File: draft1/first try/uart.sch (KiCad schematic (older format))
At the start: 24 parts, among them J1 47346-0001, U3 FT231XS-U

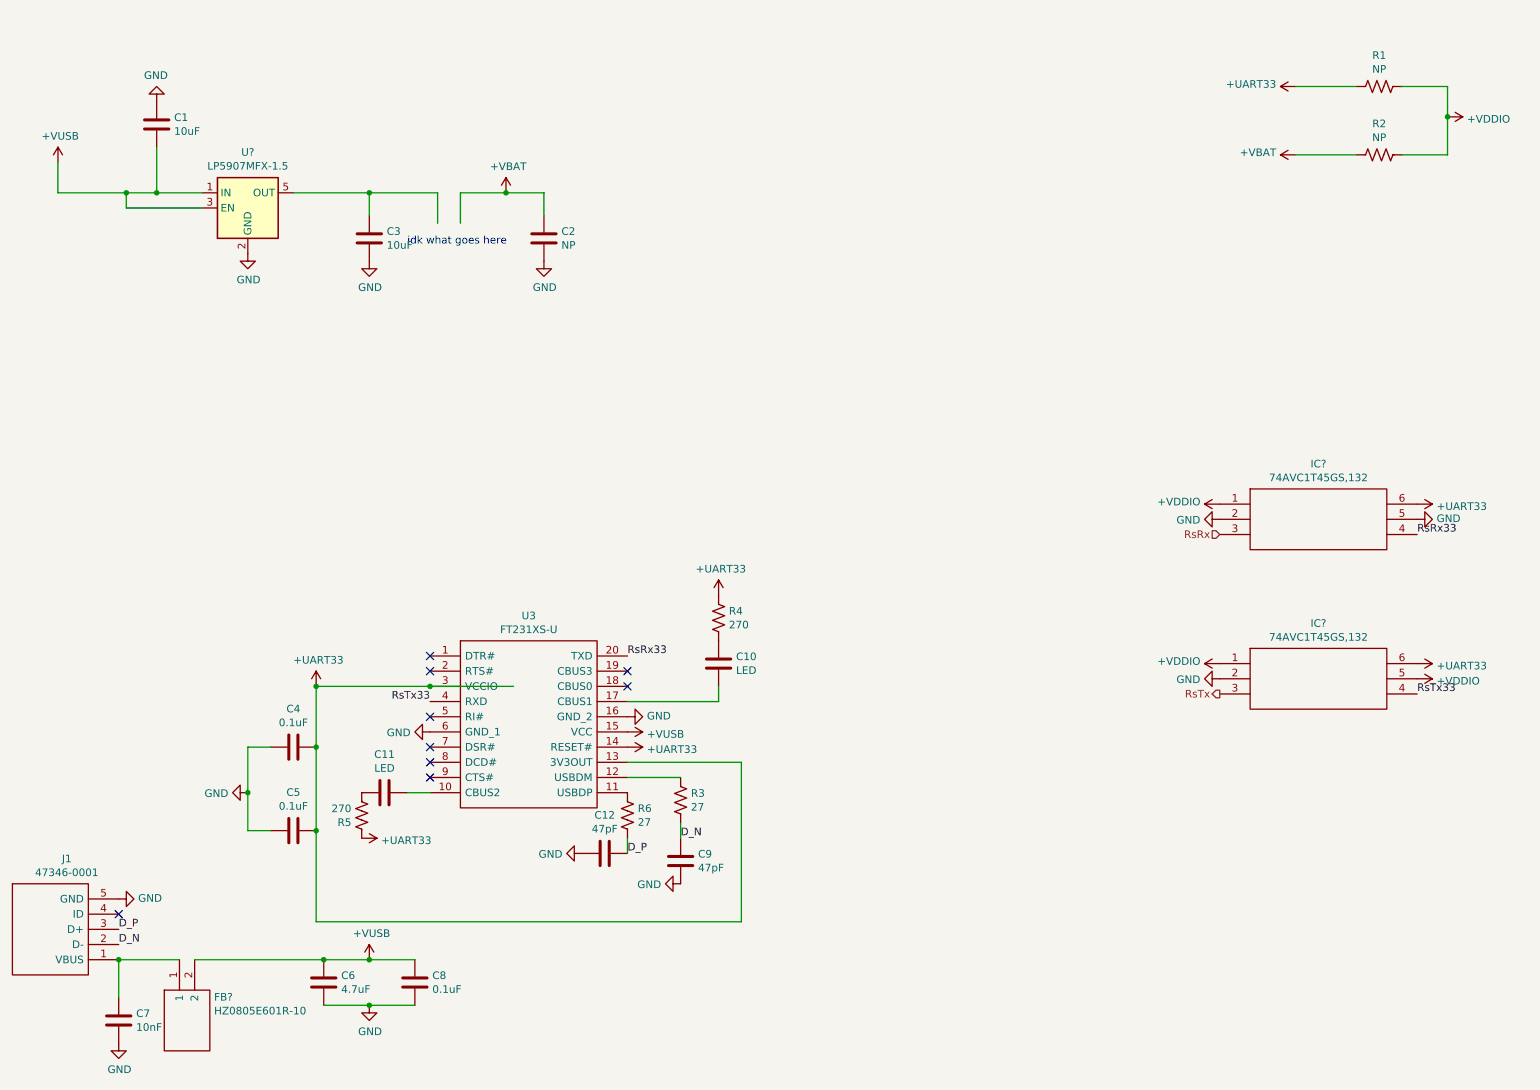
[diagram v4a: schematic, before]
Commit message: UART good enough
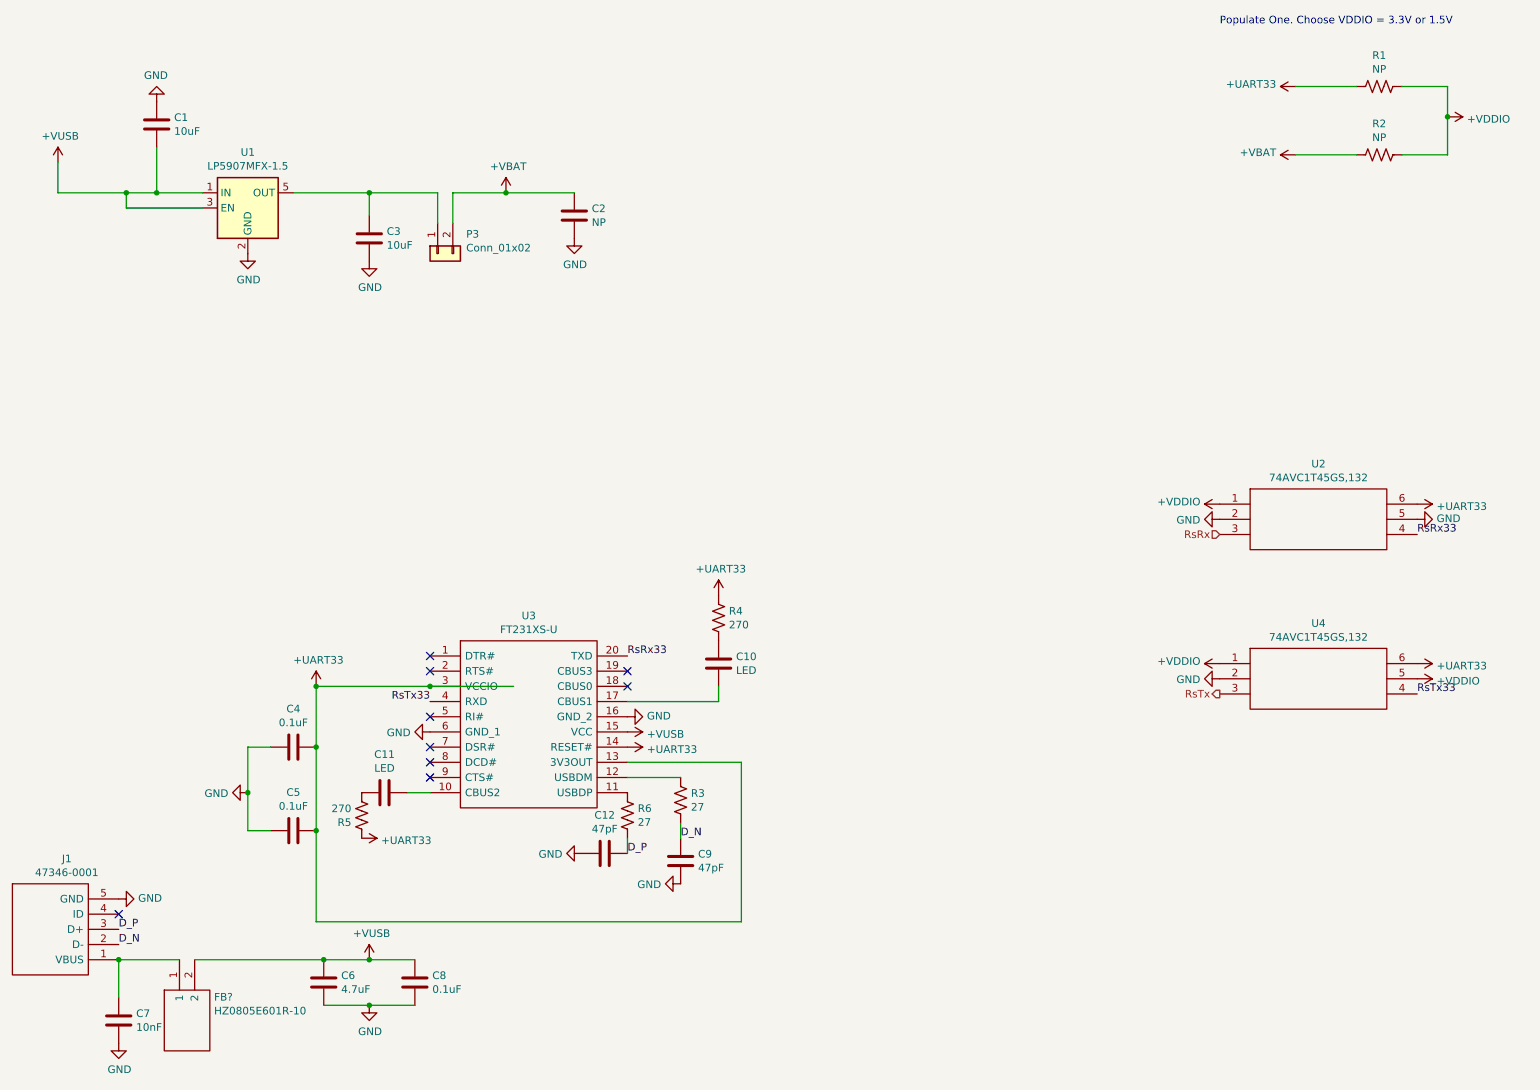
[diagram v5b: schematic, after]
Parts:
- added P3: Conn_01x02, symbol Connector_Generic:Conn_01x02
- gave numbers to parts that had none: 3
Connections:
- wire segments 46 -> 45
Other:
- note added: "Populate One. Choose VDDIO = 3.3V or 1.5V"
- note removed: "idk what goes here"
- moved on the sheet: C2
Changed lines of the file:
@@
 $EndComp
 $Comp
-L Regulator_Linear:LP5907MFX-1.5 U?
+L Regulator_Linear:LP5907MFX-1.5 U1
 U 1 1 5F39F373
 P 2250 2000
-F 0 "U?" H 2250 2367 50  0000 C CNN
+F 0 "U1" H 2250 2367 50  0000 C CNN
 F 1 "LP5907MFX-1.5" H 2250 2276 50  0000 C CNN
 F 2 "Package_TO_SOT_SMD:SOT-23-5" H 2250 2350 50  0001 C CNN
@@
 Connection ~ 1400 6950
 $Comp
-L SamacSys_Parts:74AVC1T45GS,132 IC?
+L SamacSys_Parts:74AVC1T45GS,132 U2
 U 1 1 5F3F47EB
 P 8650 3950
-F 0 "IC?" H 9300 4215 50  0000 C CNN
+F 0 "U2" H 9300 4215 50  0000 C CNN
 F 1 "74AVC1T45GS,132" H 9300 4124 50  0000 C CNN
 F 2 "74LVC1G3157GS132" H 9800 4050 50  0001 L CNN
@@
 $EndComp
 $Comp
-L SamacSys_Parts:74AVC1T45GS,132 IC?
+L SamacSys_Parts:74AVC1T45GS,132 U4
 U 1 1 5F3FAE12
 P 8650 5000
-F 0 "IC?" H 9300 5265 50  0000 C CNN
+F 0 "U4" H 9300 5265 50  0000 C CNN
 F 1 "74AVC1T45GS,132" H 9300 5174 50  0000 C CNN
 F 2 "74LVC1G3157GS132" H 9800 5100 50  0001 L CNN
@@
 L power:GND #PWR0164
 U 1 1 5F3FFFA1
-P 4200 2350
-F 0 "#PWR0164" H 4200 2100 50  0001 C CNN
-F 1 "GND" H 4205 2177 50  0000 C CNN
-F 2 "" H 4200 2350 50  0001 C CNN
-F 3 "" H 4200 2350 50  0001 C CNN
-	1    4200 2350
+P 4400 2200
+F 0 "#PWR0164" H 4400 1950 50  0001 C CNN
+F 1 "GND" H 4405 2027 50  0000 C CNN
+F 2 "" H 4400 2200 50  0001 C CNN
+F 3 "" H 4400 2200 50  0001 C CNN
+	1    4400 2200
 	1    0    0    -1
 $EndComp
@@
 L Device:C C2
 U 1 1 5F401046
-P 4200 2200
-F 0 "C2" H 4315 2246 50  0000 L CNN
-F 1 "NP" H 4315 2155 50  0000 L CNN
-F 2 "" H 4238 2050 50  0001 C CNN
-F 3 "~" H 4200 2200 50  0001 C CNN
-	1    4200 2200
+P 4400 2050
+F 0 "C2" H 4515 2096 50  0000 L CNN
+F 1 "NP" H 4515 2005 50  0000 L CNN
+F 2 "" H 4438 1900 50  0001 C CNN
+F 3 "~" H 4400 2050 50  0001 C CNN
+	1    4400 2050
 	1    0    0    -1
 $EndComp
@@
 Connection ~ 3050 1900
 Wire Wire Line
-	3650 2100 3650 1900
-Wire Wire Line
-	3650 1900 3950 1900
-Wire Wire Line
-	4200 1900 4200 2050
+	3600 2100 3600 1900
+Wire Wire Line
+	3600 1900 3950 1900
 Connection ~ 3950 1900
-Wire Wire Line
-	3950 1900 4200 1900
-Text Notes 3300 2250 0    50   ~ 0
-idk what goes here
 $Comp
 L draft1library:+UART33 #PWR0166
@@
 Wire Wire Line
 	9550 1650 9150 1650
+$Comp
+L Connector_Generic:Conn_01x02 P3
+U 1 1 5F3B48F0
+P 3500 2300
+F 0 "P3" V 3372 2112 50  0000 R CNN
+F 1 "Conn_01x02" V 3463 2112 50  0000 R CNN
+F 2 "" H 3500 2300 50  0001 C CNN
+F 3 "~" H 3500 2300 50  0001 C CNN
+	1    3500 2300
+	0    -1   1    0
+$EndComp
+Wire Wire Line
+	3950 1900 4400 1900
+Text Notes 8650 800  0    50   ~ 0
+Populate One. Choose VDDIO = 3.3V or 1.5V
 $EndSCHEMATC

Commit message: good enough top sheet
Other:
- moved on the sheet: C10, C11, C12, C4, C5, C6, C7, C8, C9, FB?, J1, R3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

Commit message: annotated
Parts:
- gave numbers to parts that had none: 1
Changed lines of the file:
@@
 	1900 6450 1900 6700
 $Comp
-L SamacSys_Parts:HZ0805E601R-10 FB?
+L SamacSys_Parts:HZ0805E601R-10 FB1
 U 1 1 5F3E1203
 P 2500 6700
-F 0 "FB?" V 2746 6472 50  0000 R CNN
+F 0 "FB1" V 2746 6472 50  0000 R CNN
 F 1 "HZ0805E601R-10" V 2837 6472 50  0000 R CNN
 F 2 "BEADC2012X90N" H 3150 6800 50  0001 L CNN

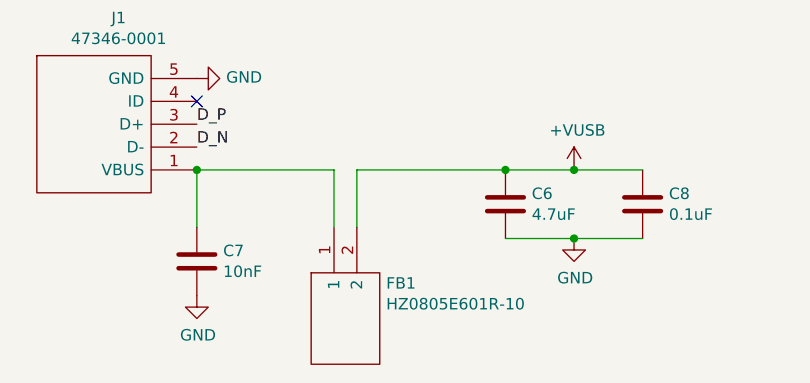
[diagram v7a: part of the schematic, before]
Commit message: renamed weird inductor
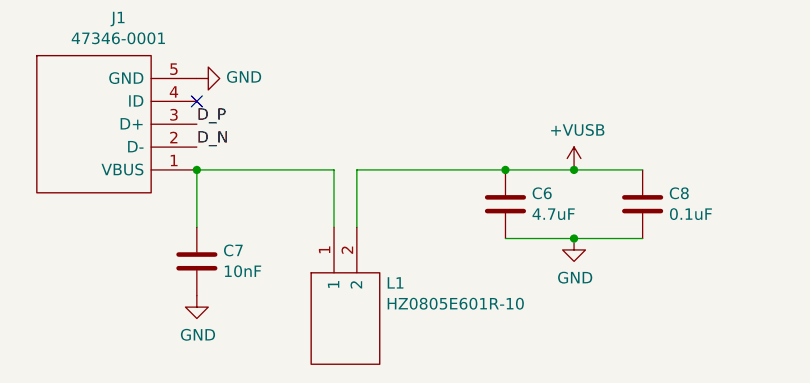
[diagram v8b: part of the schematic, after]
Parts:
- renumbered FB1 to L1
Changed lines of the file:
@@
 	1900 6450 1900 6700
 $Comp
-L SamacSys_Parts:HZ0805E601R-10 FB1
+L SamacSys_Parts:HZ0805E601R-10 L1
 U 1 1 5F3E1203
 P 2500 6700
-F 0 "FB1" V 2746 6472 50  0000 R CNN
+F 0 "L1" V 2746 6472 50  0000 R CNN
 F 1 "HZ0805E601R-10" V 2837 6472 50  0000 R CNN
 F 2 "BEADC2012X90N" H 3150 6800 50  0001 L CNN
